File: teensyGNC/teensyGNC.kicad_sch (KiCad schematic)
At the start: 32 parts, among them J1 5V_In_JST_XH, J10 TO_92_1_JST_PH, J11 TO_92_2_JST_PH, J12 TO_92_3_JST_PH, J13 TO_92_4_JST_PH, J2 ESC_1_PWM_1x03, J3 ESC_2_PWM_1x03, J4 Servo_1_PWM_1x03, J5 Servo_2_PWM_1x03, J6 7V4_In_XT30M, J7 I2C_INA_BM_JST_GH, J8 MTF_01P_JST_SH, J9 LC29H_Molex_4P, U1 LVL_Shift, U2 E28-2G4T20SX, U3 4754, U4 AP2112K-3.3, U5 DPS310, U6 Teensy4.1

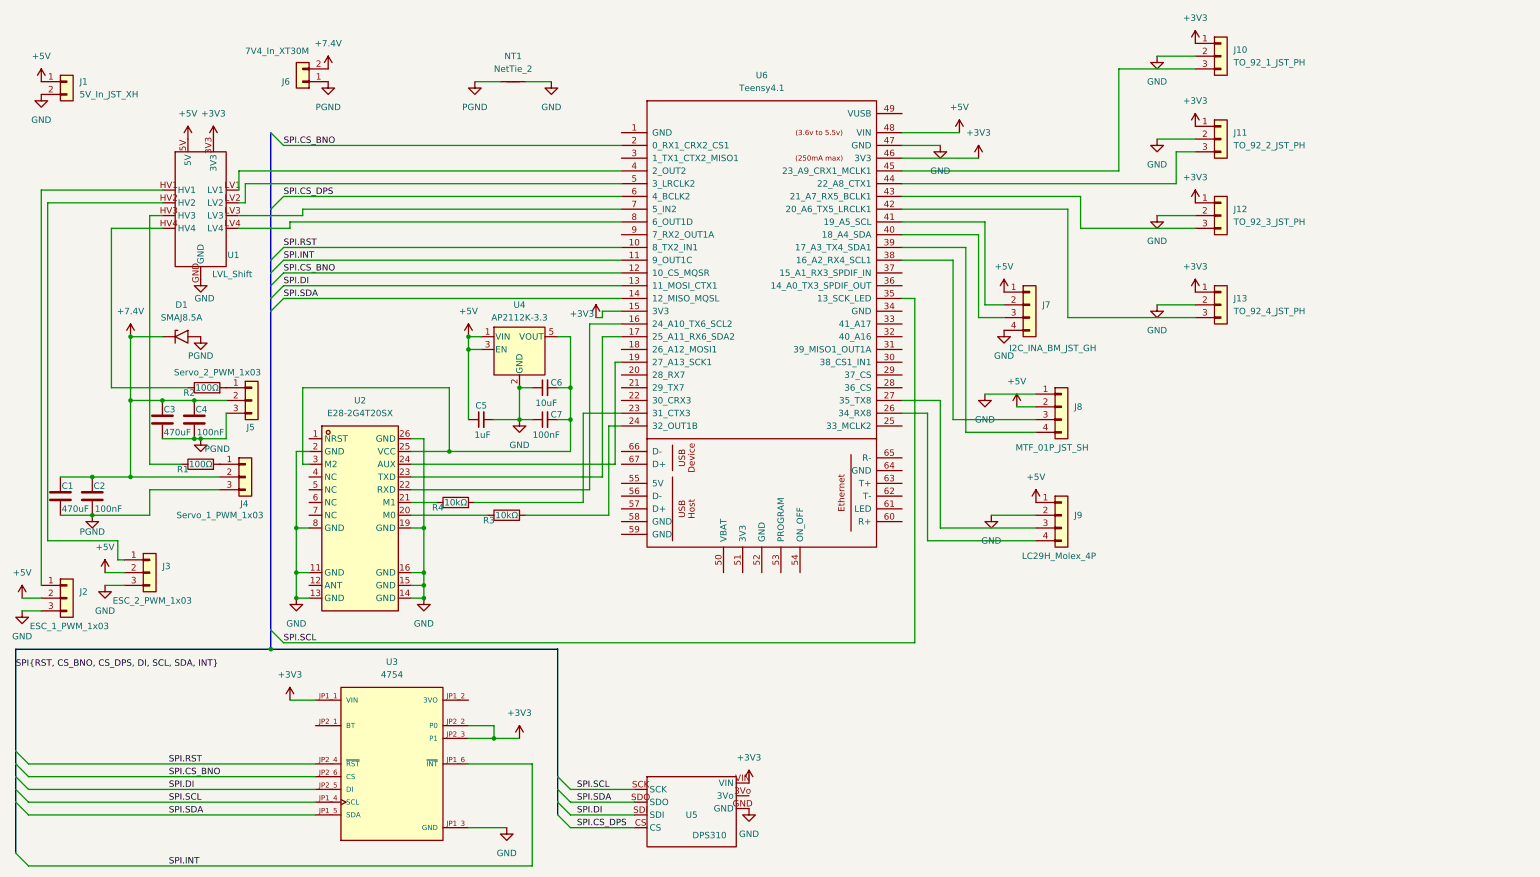
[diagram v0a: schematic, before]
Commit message: More amendments
- Added mounting holes
- Removed splits in the ground plane by removing all in1.cu plane traces
- Added pull up/down resistors (check values)
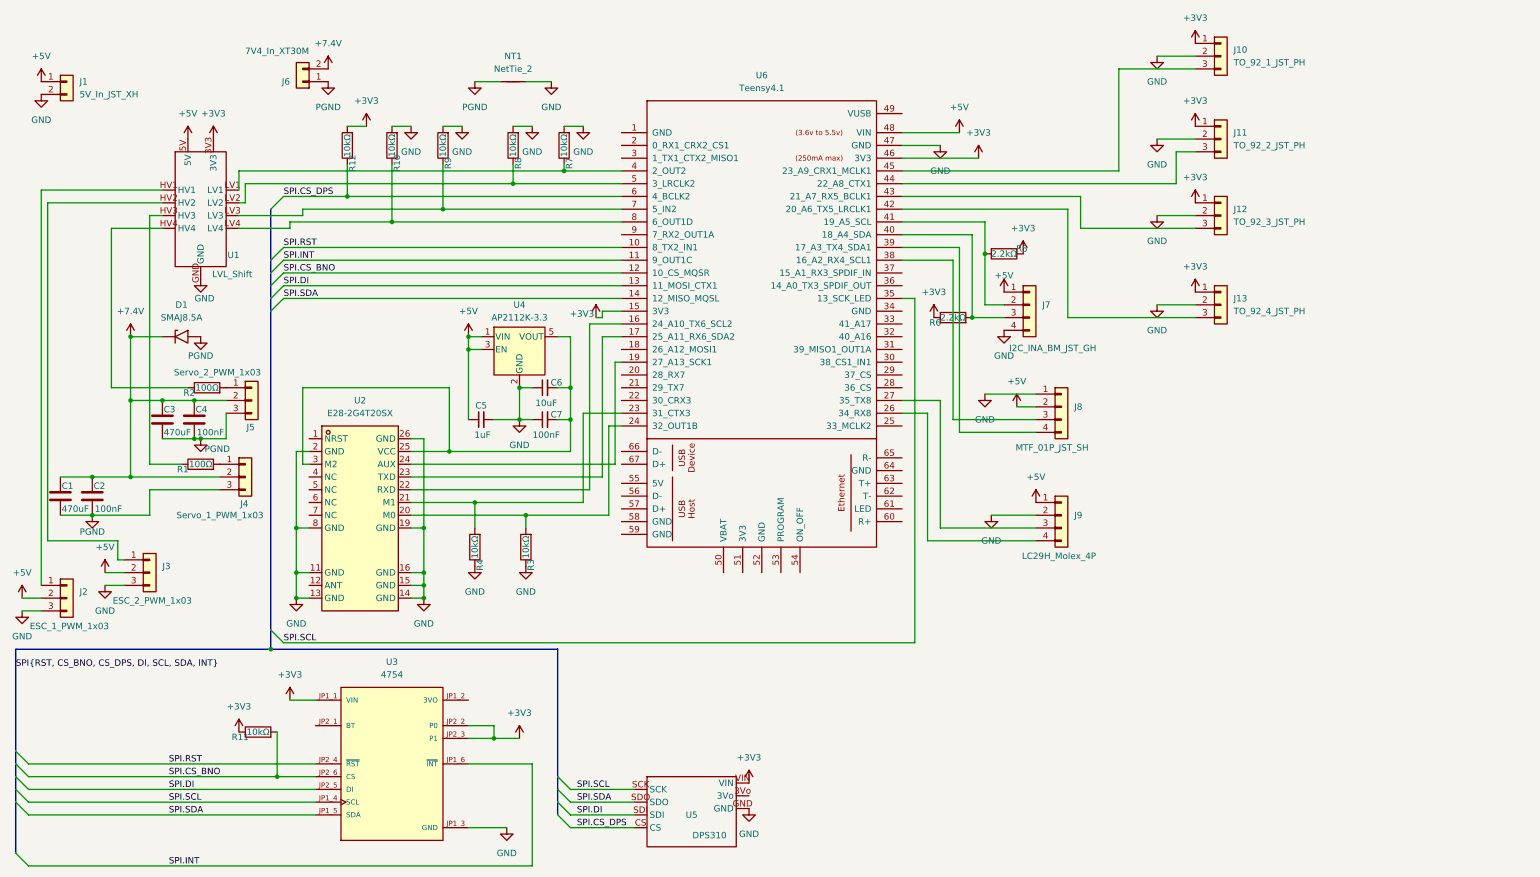
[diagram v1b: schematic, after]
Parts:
- added R10, R11, R12, R7, R8, R9: 10kΩ, Resistor_SMD:R_0603_1608Metric, symbol Device:R
- added R5, R6: 2.2kΩ, Resistor_SMD:R_0603_1608Metric, symbol Device:R
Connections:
- net +3V3: now also R11.1, R12.2, R5.1, R6.1
- net GND: now also R3.1, R4.1, R10.2, R7.2, R8.2, R9.2
- net SPI.CS_BNO: now also R11.2; no longer U6.2 (0_RX1_CRX2_CS1)
- net SPI.CS_DPS: now also R12.1
- net at U1.LV1, U6.4 (2_OUT2): now also R7.1
- net at U1.LV2, U6.5 (3_LRCLK2): now also R8.1
- net at U1.LV3, U6.7 (5_IN2): now also R9.1
- net at U1.LV4, U6.8 (6_OUT1D): now also R10.1
- net at J7.2 (Pin_2), U6.41 (19_A5_SCL): now also R5.2
- net at J7.3 (Pin_3), U6.40 (18_A4_SDA): now also R6.2
- net at U2.20 (M0): now also R3.2, U6.24 (32_OUT1B); no longer R3.1
- net at R4.2, U6.23 (31_CTX3): now also U2.21 (M1)
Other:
- moved on the sheet: R3, R4

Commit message: Moved LC29H onboard and to the top of the board
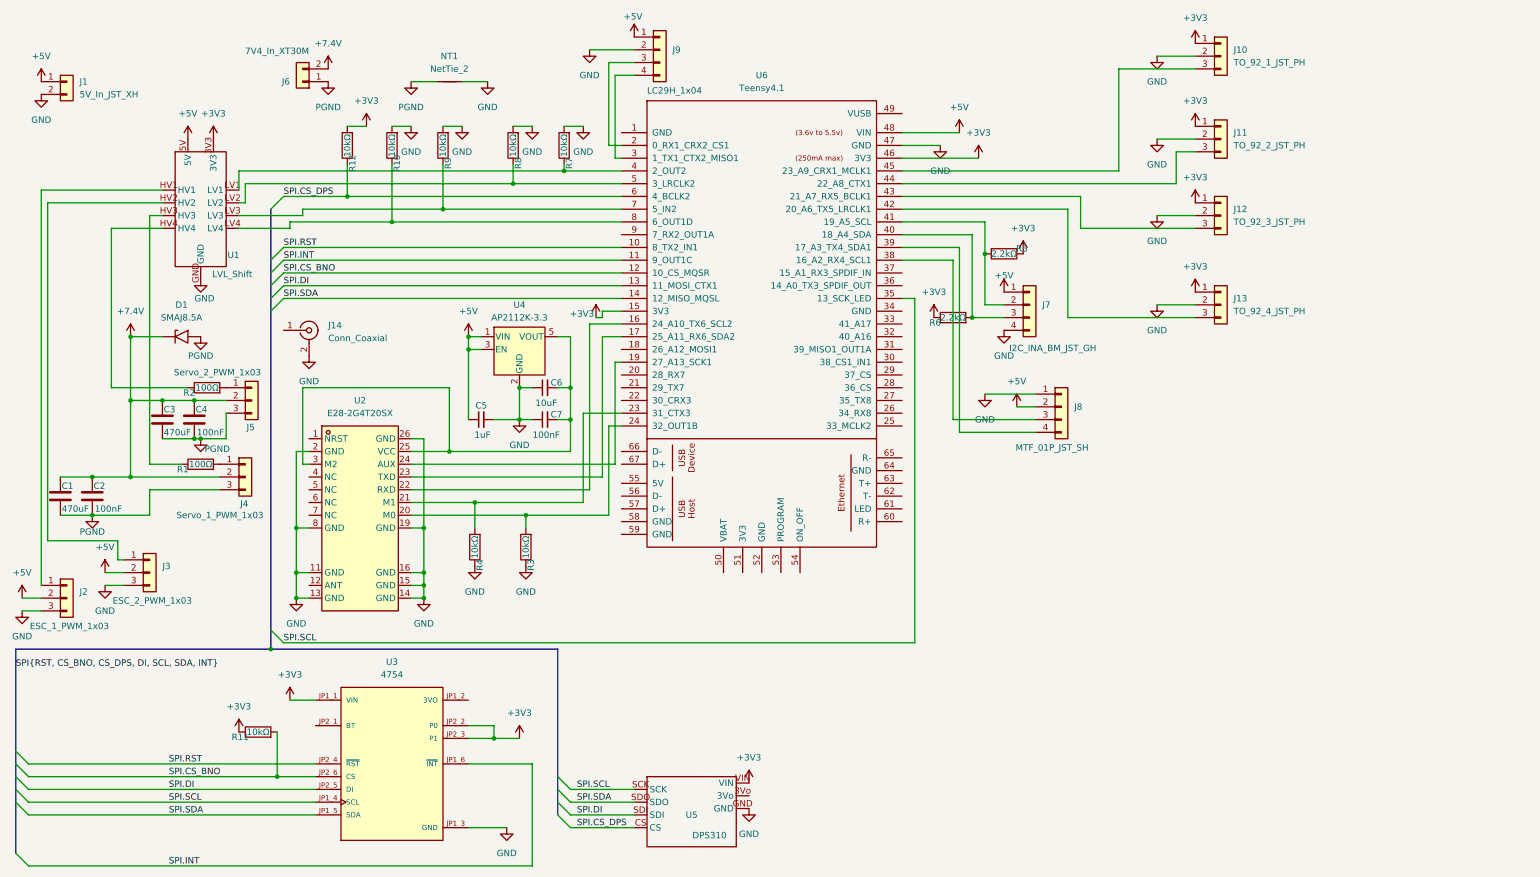
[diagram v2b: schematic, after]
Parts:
- added J14: Conn_Coaxial, Connector_Coaxial:SMA_Amphenol_132203-12_Horizontal, symbol Connector:Conn_Coaxial
- J9: value LC29H_Molex_4P -> LC29H_1x04; footprint Connector_PinHeader_2.54mm:PinHeader_1x04_P2.54mm_Horizontal -> Connector_PinHeader_2.54mm:PinHeader_1x04_P2.54mm_Vertical
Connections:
- net GND: now also J14.2 (Ext)
- net at J9.3 (Pin_3): now also U6.2 (0_RX1_CRX2_CS1); no longer U6.27 (35_TX8)
- net at J9.4 (Pin_4): now also U6.3 (1_TX1_CTX2_MISO1); no longer U6.26 (34_RX8)
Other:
- moved on the sheet: J9, NT1

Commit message: Suggestions from Jack pt 1
- LVL shifter removed, both servo and escs tested to be OK with 3v3
- split plane removed, seems to be archaic method, and they haven't seen issues that require split ground planes to fix
- Trace for antennae added, need to add proper components for the pi matching network and trace sizes
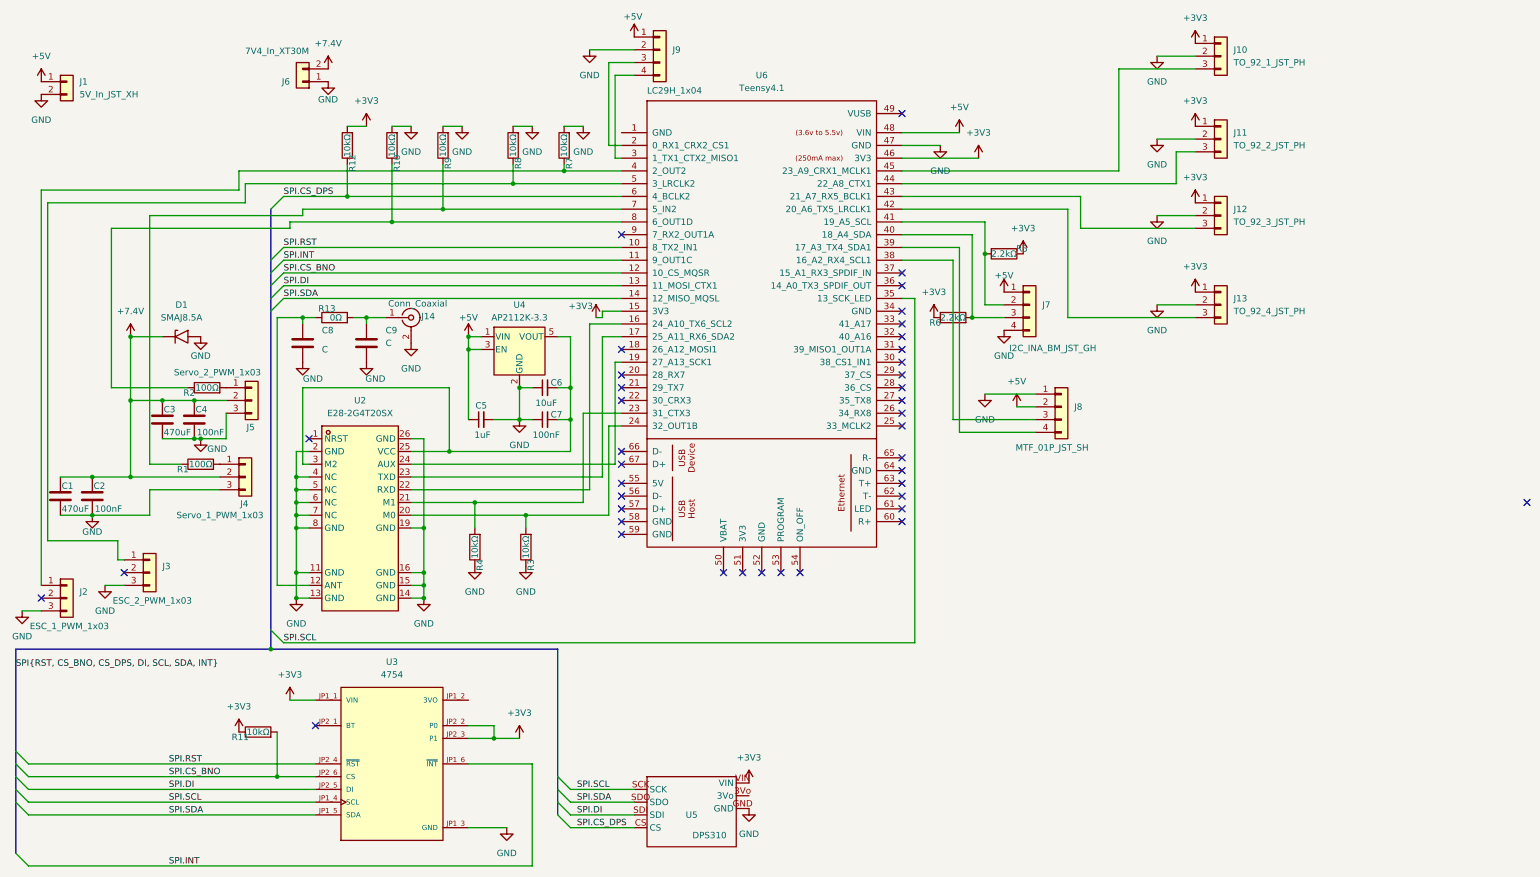
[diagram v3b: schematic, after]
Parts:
- removed NT1: NetTie_2, NetTie:NetTie-2_SMD_Pad2.0mm, symbol Device:NetTie_2
- removed U1: LVL_Shift, teensyGNC_footprints:MH_level_shifter, symbol teensyGNC_symbols:5V_3V3_level_shifter
- added C8, C9: C, Capacitor_SMD:C_0402_1005Metric, symbol Device:C
- added R13: 0Ω, Resistor_SMD:R_0402_1005Metric, symbol Device:R
- J6: footprint Connector_AMASS:AMASS_XT30PW-M_1x02_P2.50mm_Horizontal -> Connector_AMASS:AMASS_XT30UPB-M_1x02_P5.0mm_Vertical
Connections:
- net PGND is gone; now on net GND: C1.2, C2.2, C3.2, C4.2, D1.2 (A2), J4.3 (Pin_3), J5.3 (Pin_3), J6.1 (Pin_1)
- net +5V: no longer J2.2 (Pin_2), J3.2 (Pin_2)
- net GND: now also U2.4 (NC), U2.5 (NC), U2.6 (NC), U2.7 (NC), C8.2, C9.2
- net at R10.1, U6.8 (6_OUT1D): now also R2.1
- net at J2.1 (Pin_1): now also R7.1, U6.4 (2_OUT2)
- net at J3.1 (Pin_1): now also R8.1, U6.5 (3_LRCLK2)
- net at R1.1: now also R9.1, U6.7 (5_IN2)
- net at J14.1 (In): now also C9.1, R13.2
- net at U2.12 (ANT): now also C8.1, R13.1
- no-connect marks 0 -> 41
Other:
- moved on the sheet: J14

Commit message: Suggestions from Jack part 2 + some other changes
- Ground pours on signal planes
- Capacitors changed to flatter versions
- Connector movements for teensy usb clearance
- Silkscreen labels
- Ran DRC; no errors just text warnings
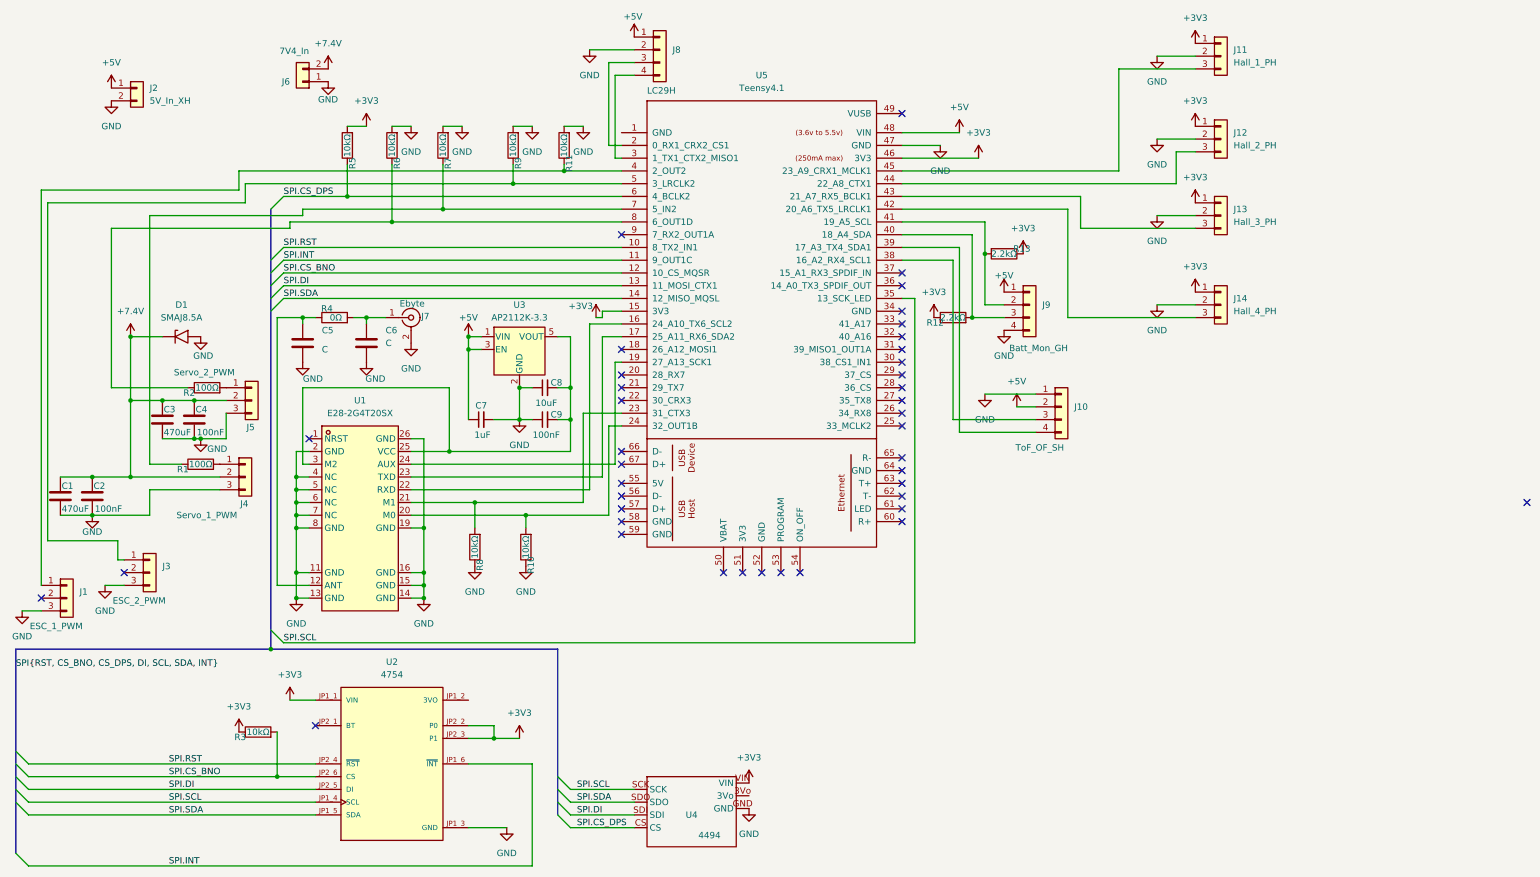
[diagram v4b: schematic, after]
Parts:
- C1, C3: footprint Capacitor_SMD:CP_Elec_6.3x5.4 -> Capacitor_Tantalum_SMD:CP_EIA-7343-43_Kemet-X
- J1: renamed from J2; value ESC_1_PWM_1x03 -> ESC_1_PWM
- J10: renamed from J8; value MTF_01P_JST_SH -> ToF_OF_SH
- J11: renamed from J10; value TO_92_1_JST_PH -> Hall_1_PH
- J12: renamed from J11; value TO_92_2_JST_PH -> Hall_2_PH
- J13: renamed from J12; value TO_92_3_JST_PH -> Hall_3_PH
- J14: renamed from J13; value TO_92_4_JST_PH -> Hall_4_PH
- J2: renamed from J1; value 5V_In_JST_XH -> 5V_In_XH
- J3: value ESC_2_PWM_1x03 -> ESC_2_PWM
- J4: value Servo_1_PWM_1x03 -> Servo_1_PWM
- J5: value Servo_2_PWM_1x03 -> Servo_2_PWM
- J6: value 7V4_In_XT30M -> 7V4_In
- J7: renamed from J14; value Conn_Coaxial -> Ebyte
- J8: renamed from J9; value LC29H_1x04 -> LC29H
- J9: renamed from J7; value I2C_INA_BM_JST_GH -> Batt_Mon_GH
- U4: renamed from U5; value DPS310 -> 4494
- renumbered C8 to C5, C9 to C6, C5 to C7, C6 to C8, C7 to C9, R3 to R10, R7 to R11, R6 to R12, R5 to R13, R11 to R3, R13 to R4, R12 to R5, R10 to R6, R9 to R7, R4 to R8, R8 to R9, U2 to U1, U3 to U2, U4 to U3, U6 to U5
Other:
- moved on the sheet: J2

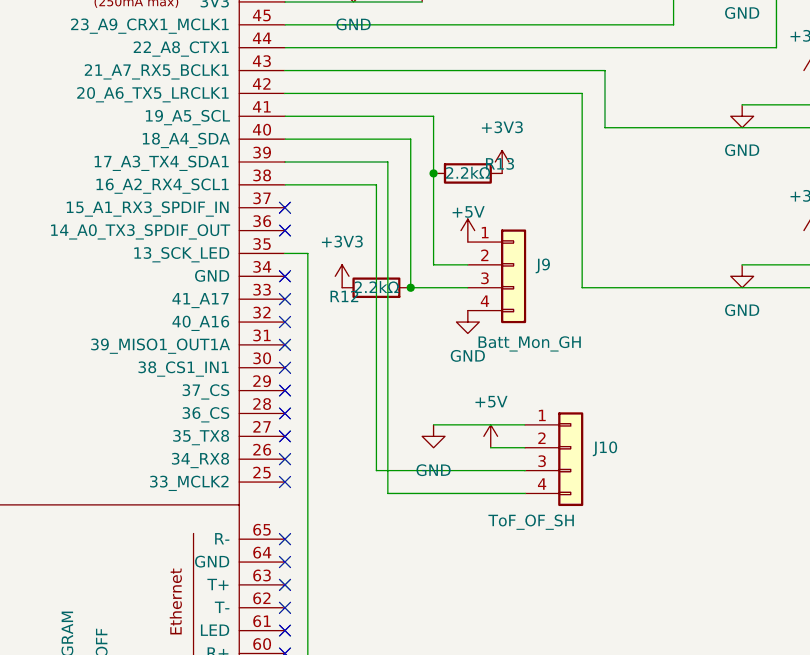
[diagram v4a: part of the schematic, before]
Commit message: DRC passed and offboard connector pinouts checked
- All connectors vertical now for better cable management
- LCSC numbers added as fields for jlcpcb assembly
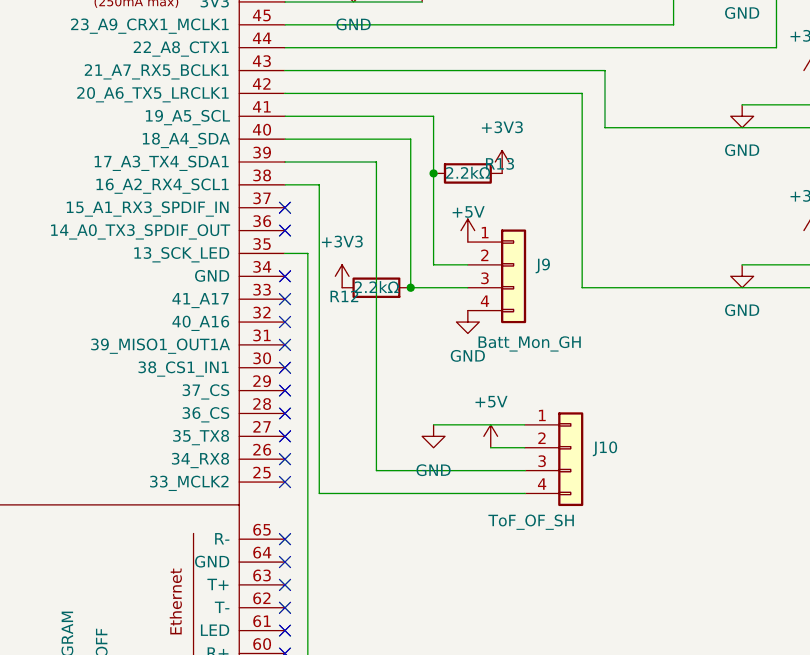
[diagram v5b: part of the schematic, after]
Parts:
- C1, C3: LCSC Part (none) -> C7234
- C2, C4, C9: LCSC Part (none) -> C14663
- C7: LCSC Part (none) -> C559769
- C8: LCSC Part (none) -> C109457
- D1: LCSC Part (none) -> C135018
- J10: LCSC Part (none) -> C160390
- J11, J12, J13, J14: LCSC Part (none) -> C131339
- J2: LCSC Part (none) -> C158012
- J6: LCSC Part (none) -> C428721
- J7: LCSC Part (none) -> C6962402
- J9: LCSC Part (none) -> C161692
- R1, R2: LCSC Part (none) -> C122970
- R10, R11, R5, R6, R7, R8, R9: LCSC Part (none) -> C5362358
- R12, R13: LCSC Part (none) -> C4190
- R4: LCSC Part (none) -> C17168
- U3: LCSC Part (none) -> C51118
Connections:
- net at J10.3 (Pin_3): now also U5.39 (17_A3_TX4_SDA1); no longer U5.38 (16_A2_RX4_SCL1)
- net at J10.4 (Pin_4): now also U5.38 (16_A2_RX4_SCL1); no longer U5.39 (17_A3_TX4_SDA1)
